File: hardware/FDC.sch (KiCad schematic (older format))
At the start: 6 parts, among them J1 EXPANSION, J2 Floppy, U1 FDC37C78, X1 24MHz, X2 CXO_DIP14

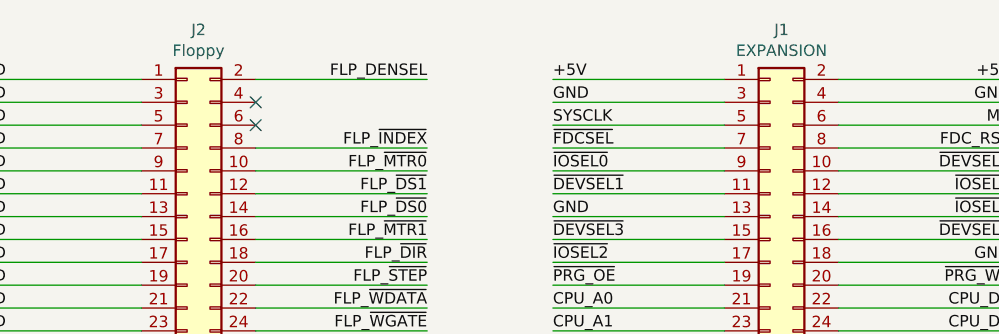
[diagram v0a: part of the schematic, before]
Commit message: Update FDC.sch
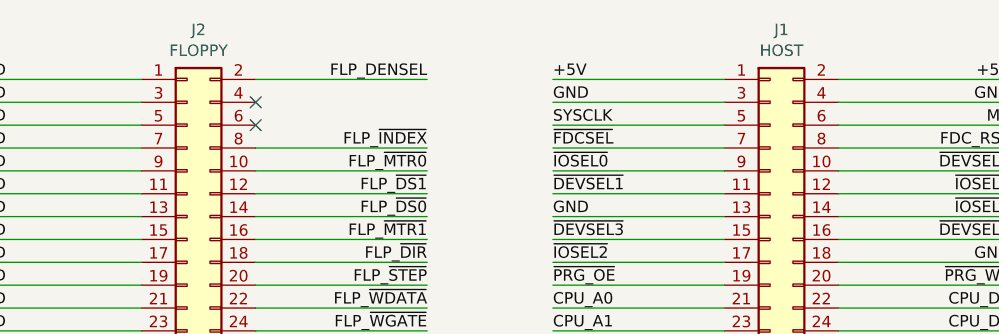
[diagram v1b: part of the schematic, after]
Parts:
- J1: value EXPANSION -> HOST
- J2: value Floppy -> FLOPPY
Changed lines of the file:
@@
 P 5550 2250
 F 0 "J2" H 5600 3267 50  0000 C CNN
-F 1 "Floppy" H 5600 3176 50  0000 C CNN
+F 1 "FLOPPY" H 5600 3176 50  0000 C CNN
 F 2 "Connector_PinHeader_2.54mm:PinHeader_2x17_P2.54mm_Vertical" H 5550 2250 50  0001 C CNN
 F 3 "~" H 5550 2250 50  0001 C CNN
@@
 AR Path="/75E32237/76935B71" Ref="J1"  Part="1"
 F 0 "J1" H 8150 3467 50  0000 C CNN
-F 1 "EXPANSION" H 8150 3376 50  0000 C CNN
+F 1 "HOST" H 8150 3376 50  0000 C CNN
 F 2 "Connector_PinHeader_2.54mm:PinHeader_2x20_P2.54mm_Vertical" H 8100 2350 50  0001 C CNN
 F 3 "~" H 8100 2350 50  0001 C CNN
